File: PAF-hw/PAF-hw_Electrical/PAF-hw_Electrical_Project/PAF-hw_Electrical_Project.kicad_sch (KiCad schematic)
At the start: 0 parts

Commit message: Initial commit of schematic. Added ESP32 module. MicroUSB, and USB-C circuits to schematic.
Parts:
- added C1, C2: 10uF, CAPC2012X145N, symbol SamacSys_Parts:CL21A106KAYNNNE
- added D1, D5: 1N5819HWQ-7-F, SOD3716X145N, symbol SamacSys_Parts:1N5819HWQ-7-F
- added D2, D3, D4, D6, D7, D8: ESDLC5V0D3B-TP, SOD2512X115N, symbol SamacSys_Parts:ESDLC5V0D3B-TP
- added J1: USB_B_Micro, symbol Connector:USB_B_Micro
- added J2: USB_C_Receptacle_USB2.0_16P, symbol Connector:USB_C_Receptacle_USB2.0_16P
- added R1, R2: 5.1k, symbol Device:R
- added U1: ESP32-S3-WROOM-1, PCM_Espressif:ESP32-S3-WROOM-1, symbol PCM_Espressif:ESP32-S3-WROOM-1
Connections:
- new net: J2.B5 (CC2), R1.1
- new net: J2.A5 (CC1), R2.1
- new net +5V: C1.1, C2.1, D1.1 (K), D5.1 (K)
- new net D_N: D4.1 (K1), J1.2 (D-)
- new net D_P: D3.1 (K1), J1.3 (D+)
- new net EN: U1.3 (EN)
- new net ESP32_3V3: U1.2 (3V3)
- new net GND: C1.2, C2.2, D2.2 (K2), D3.2 (K2), D4.2 (K2), D6.2 (K2), D7.2 (K2), D8.2 (K2), J1.5 (GND), J1.6 (Shield), J2.A1 (GND), J2.A12 (GND), J2.B1 (GND), J2.B12 (GND), J2.S1 (SHIELD), R1.2, R2.2, U1.1 (GND), U1.40 (GND), U1.41 (GND)
- new net GPIO19/D_N: D8.1 (K1), J2.A7 (D-), J2.B7 (D-), U1.13 (GPIO19/U1RTS/ADC2_CH8/CLK_OUT2/USB_D-)
- new net GPIO20/D_P: D7.1 (K1), J2.A6 (D+), J2.B6 (D+), U1.14 (GPIO20/U1CTS/ADC2_CH9/CLK_OUT1/USB_D+)
- new net VBUS: D1.2 (A), D2.1 (K1), J1.1 (VBUS)
- new net VBUS_B: D5.2 (A), D6.1 (K1), J2.A4 (VBUS), J2.A9 (VBUS), J2.B4 (VBUS), J2.B9 (VBUS)
- no-connect marks 0 -> 3

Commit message: Added LDO and reset/boot swtiches to schematic.
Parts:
- added C3, C7: 10uF, CAPC2012X145N, symbol SamacSys_Parts:CL21A106KAYNNNE
- added C4, C5, C6, C8: 0.1uF, C0603, symbol SamacSys_Parts:C0603C104K5RACTU
- added IC1: NCP1117IST33T3G, SOT230P700X180-4N, symbol SamacSys_Parts:NCP1117IST33T3G
- added LED1: RED LED, SMLLX0805SRCTR, symbol SamacSys_Parts:SML-LX0805SRC-TR
- added R3: 5.1k, symbol Device:R
- added S1, S2: PTS647SK38SMTR2_LFS, PTS647SM38SMTR2LFS, symbol SamacSys_Parts:PTS647SK38SMTR2_LFS
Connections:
- net +5V: now also C3.1, C4.1, IC1.3 (INPUT_1)
- net EN: now also C6.2, S2.1 (NO_1), S2.2 (NO_2)
- net GND: now also R1.1, R2.1, C3.2, C4.2, C5.1, C6.1, C7.2, C8.2, IC1.1 (ADJUST/GROUND), LED1.2 (K), S1.3 (COM_1), S1.4 (COM_2), S2.3 (COM_1), S2.4 (COM_2); no longer R1.2, R2.2
- net at J2.B5 (CC2): now also R1.2; no longer R1.1
- net GPIO0/BOOT: now reaches U1.27 (GPIO0/BOOT)
- net GPIO0/BOOT: now also C5.2, S1.1 (NO_1), S1.2 (NO_2)
- net at J2.A5 (CC1): now also R2.2; no longer R2.1
- net ESP32_3V3 renamed +3.3V
- net +3.3V: now also C7.1, C8.1, IC1.2 (OUTPUT), IC1.4 (INPUT_2), R3.1
- new net: LED1.1 (A), R3.2
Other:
- moved on the sheet: C1, R1, R2, U1

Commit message: Added USB to UART and automatic boot logic to schematic.
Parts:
- added C10, C12: 10uF, CAPC2012X145N, symbol SamacSys_Parts:CL21A106KAYNNNE
- added C11: 0.1uF, C0603, symbol SamacSys_Parts:C0603C104K5RACTU
- added C13, C9: 1uF, CAPC1608X90N, symbol SamacSys_Parts:CL10B105KO8NNNC
- added IC2: CP2102N-A02-GQFN28R, QFN50P500X500X80-29N-D, symbol SamacSys_Parts:CP2102N-A02-GQFN28R
- added Q1, Q2: BC818-25, SOT95P230X110-3N, symbol SamacSys_Parts:BC818-25
- added R10, R12, R4, R8: 10k, symbol Device:R
- added R11, R13, R14, R15, R9: 0, symbol Device:R
- added R5: 22.1k, symbol Device:R
- added R6: 47.5k, symbol Device:R
- added R7: 1k, symbol Device:R
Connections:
- net +3.3V: now also C10.1, C11.1, C12.1, IC2.6 (VDD), IC2.7 (VREGIN), R15.1, R15.2, R4.1, R7.1
- net D_N: now also IC2.5 (D-)
- net D_P: now also IC2.4 (D+)
- net EN: now also C6.1, C9.1, R13.1, R4.2; no longer C6.2
- net GND: now also C6.2, C10.2, C11.2, C12.2, C13.2, C9.2, IC2.29 (GND_2), IC2.3 (GND_1), R6.2, R8.1; no longer C6.1
- net GPIO0/BOOT: now also R14.1
- net VBUS: now also R5.2
- net U0RXD: now reaches U1.36 (U0RXD/GPIO44/CLK_OUT2)
- net U0RXD: now also R9.1
- net U0TXD: now reaches U1.37 (U0TXD/GPIO43/CLK_OUT1)
- net U0TXD: now also R11.1
- new net: IC2.26 (TXD), R9.2
- new net: Q2.1 (B), R12.1
- new net: Q2.3 (C), R14.2
- new net: IC2.9 (RSTB), R7.2
- new net: IC2.11 (SUSPENDB), R8.2
- new net: IC2.25 (RXD), R11.2
- new net: C13.1, IC2.8 (VBUS), R5.1, R6.1
- new net: Q1.1 (B), R10.1
- new net: Q1.3 (C), R13.2
- new net DTR: IC2.28 (DTR), Q2.2 (E), R10.2
- new net RTS: IC2.24 (RTS), Q1.2 (E), R12.2
- no-connect marks 3 -> 18
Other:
- moved on the sheet: C5, C6, S1, S2, U1

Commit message: Added 12V input to the schematic, and simulated soft start circuit.
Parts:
- added C14: 10uF, CAPC2012X145N, symbol SamacSys_Parts:CL21A106KAYNNNE
- added D9: ESD12VD3B-TP, SOD2512X115N, symbol SamacSys_Parts:ESD12VD3B-TP
- added J3: Barrel_Jack_Switch, symbol Connector:Barrel_Jack_Switch
- added LED2: GREEN LED, LEDC2012X120N, symbol SamacSys_Parts:LTST-C170GKT
- added R16: 300, symbol Device:R
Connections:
- net GND: now also C14.2, D9.2, J3.2, J3.3, LED2.1 (K)
- net GPIO21: now reaches U1.23 (GPIO21)
- net GPIO21: now also R16.2
- new net: LED2.2 (A), R16.1
- new net +12V: C14.1, D9.1, J3.1
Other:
- moved on the sheet: C1, C10, C11, C12, C13, C2, C3, C4, C5, C6, C7, C8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

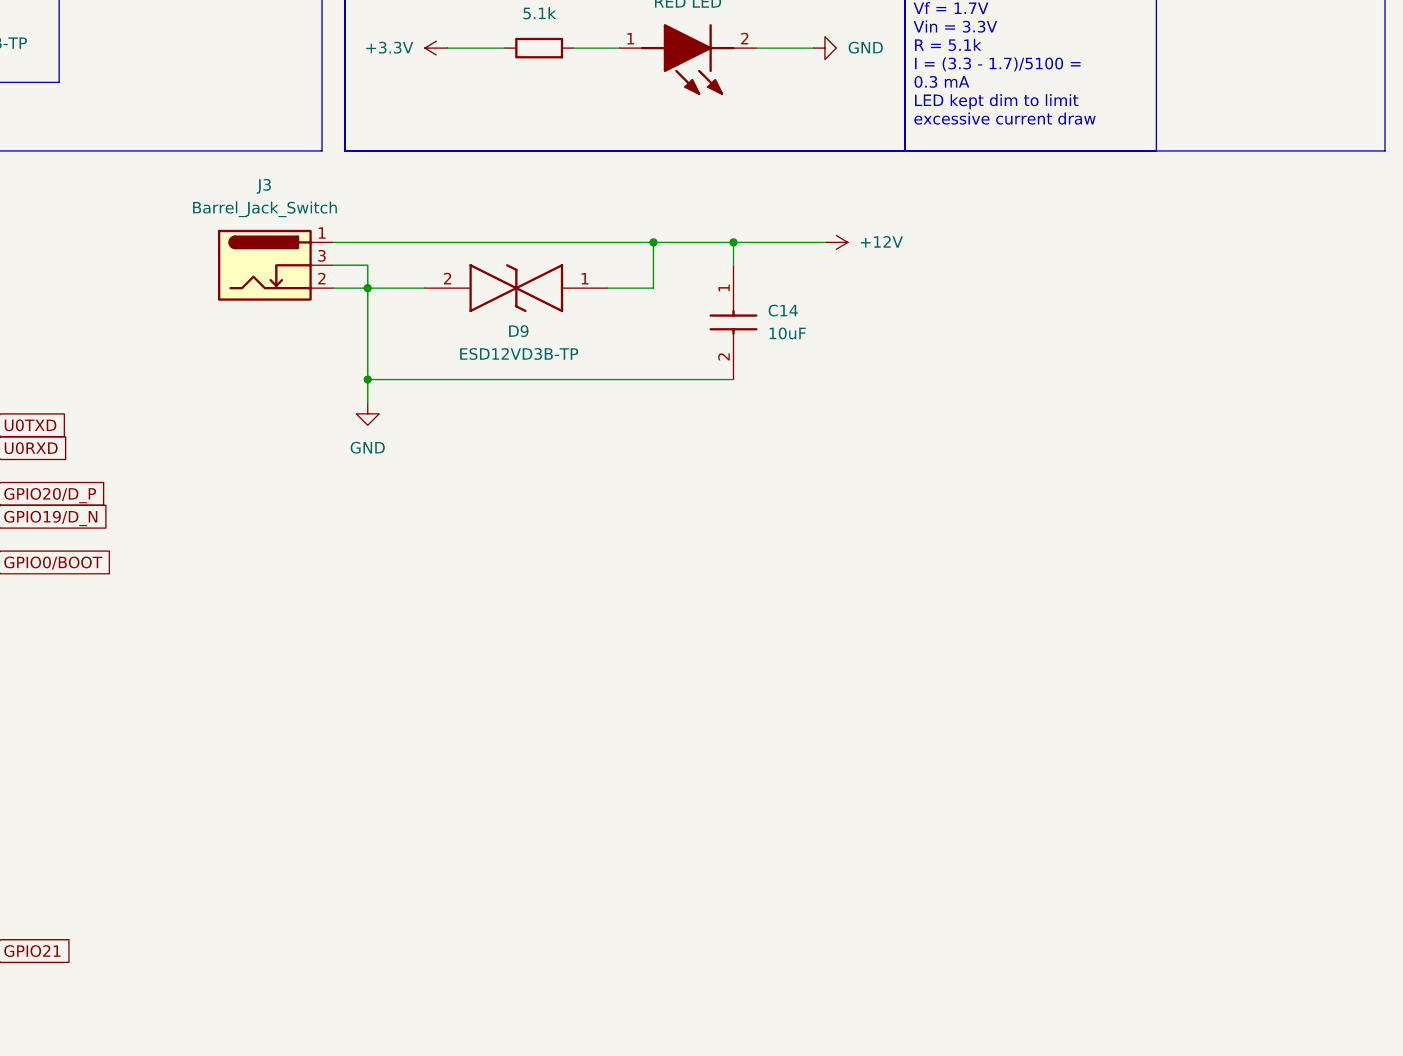
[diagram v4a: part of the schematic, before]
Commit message: Added soft start on 12V rail to schematic.
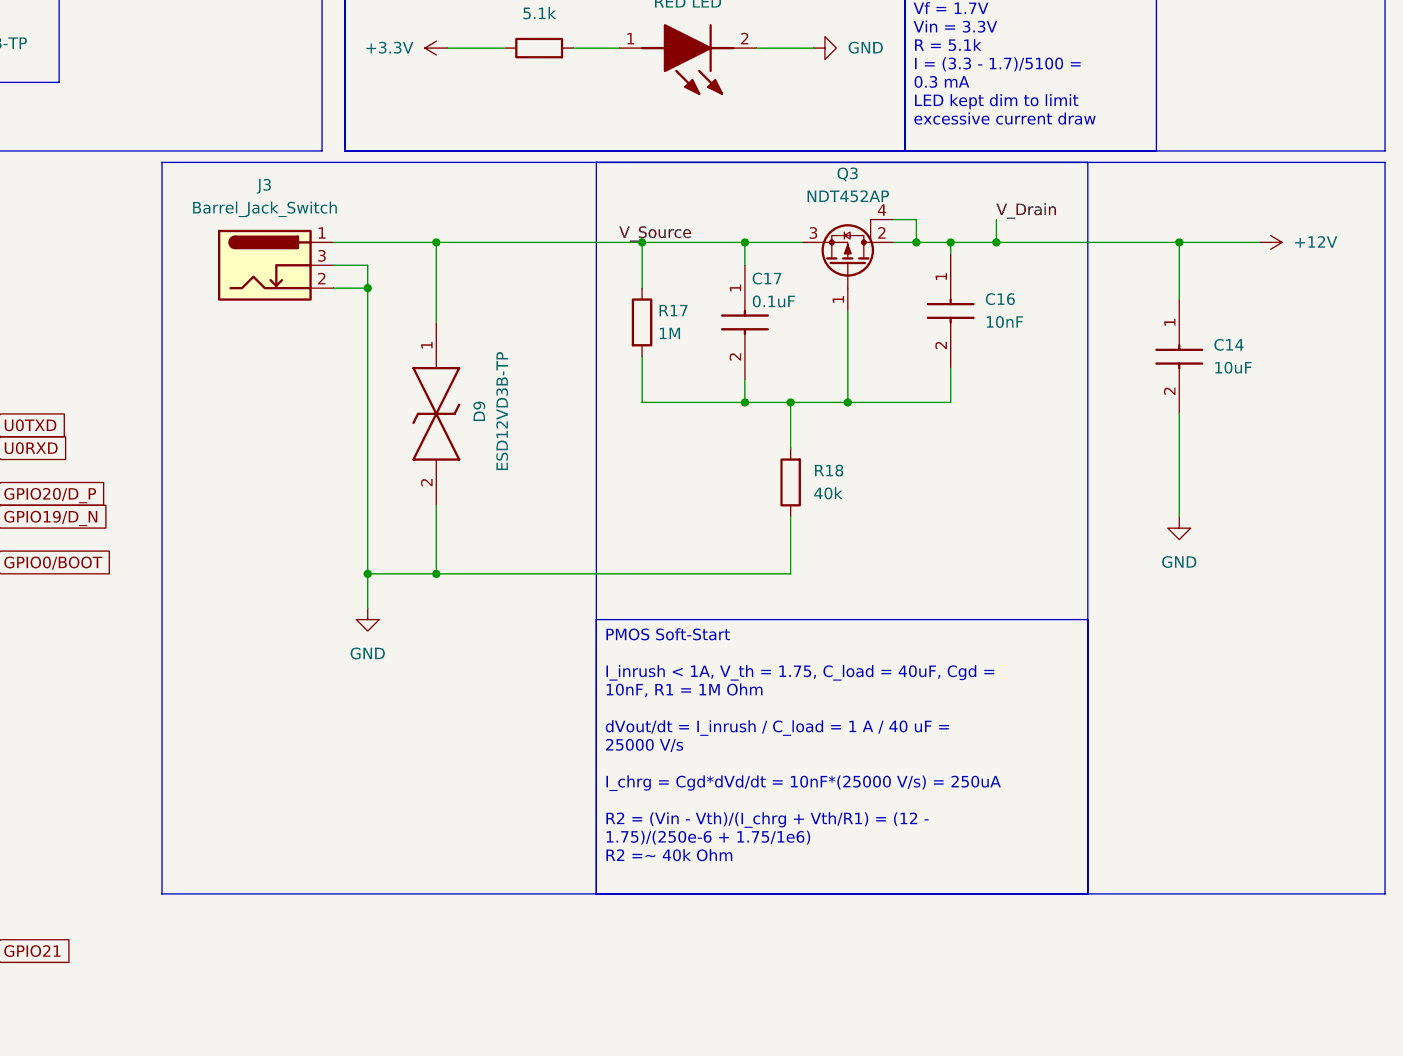
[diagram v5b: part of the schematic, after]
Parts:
- added C16: 10nF, CAPC1005X70N, symbol SamacSys_Parts:GRM155R71E103KA01D
- added C17: 0.1uF, C0603, symbol SamacSys_Parts:C0603C104K5RACTU
- added Q3: NDT452AP, SamacSys_Parts:SOT230P700X180-4N, symbol Transistor_FET:Q_PMOS_GDSD
- added R17: 1M, symbol Device:R
- added R18: 40k, symbol Device:R
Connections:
- net +12V: now also C16.1, Q3.2 (D), Q3.4 (D); no longer D9.1, J3.1
- net GND: now also R18.1
- new net: C16.2, C17.2, Q3.1 (G), R17.2, R18.2
- new net V_Source: C17.1, D9.1, J3.1, Q3.3 (S), R17.1
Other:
- moved on the sheet: D9

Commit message: Added 12V to 5V switching regulator to schematic and converted all modules to hiearchal schematics.
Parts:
- removed C1, C12, C14, C2, C3, C7: 10uF, CAPC2012X145N, symbol SamacSys_Parts:CL21A106KAYNNNE
- removed C13, C9: 1uF, CAPC1608X90N, symbol SamacSys_Parts:CL10B105KO8NNNC
- removed C16: 10nF, CAPC1005X70N, symbol SamacSys_Parts:GRM155R71E103KA01D
- removed C17, C4, C5, C6, C8: 0.1uF, C0603, symbol SamacSys_Parts:C0603C104K5RACTU
- removed D1, D5: 1N5819HWQ-7-F, SOD3716X145N, symbol SamacSys_Parts:1N5819HWQ-7-F
- removed D2, D3, D4, D6, D7, D8: ESDLC5V0D3B-TP, SOD2512X115N, symbol SamacSys_Parts:ESDLC5V0D3B-TP
- removed D9: ESD12VD3B-TP, SOD2512X115N, symbol SamacSys_Parts:ESD12VD3B-TP
- removed IC1: NCP1117IST33T3G, SOT230P700X180-4N, symbol SamacSys_Parts:NCP1117IST33T3G
- removed IC2: CP2102N-A02-GQFN28R, QFN50P500X500X80-29N-D, symbol SamacSys_Parts:CP2102N-A02-GQFN28R
- removed J1: USB_B_Micro, symbol Connector:USB_B_Micro
- removed J2: USB_C_Receptacle_USB2.0_16P, symbol Connector:USB_C_Receptacle_USB2.0_16P
- removed J3: Barrel_Jack_Switch, symbol Connector:Barrel_Jack_Switch
- removed LED1: RED LED, SMLLX0805SRCTR, symbol SamacSys_Parts:SML-LX0805SRC-TR
- removed Q1, Q2: BC818-25, SOT95P230X110-3N, symbol SamacSys_Parts:BC818-25
- removed Q3: NDT452AP, SamacSys_Parts:SOT230P700X180-4N, symbol Transistor_FET:Q_PMOS_GDSD
- removed R1, R2, R3: 5.1k, symbol Device:R
- removed R10, R12, R4, R8: 10k, symbol Device:R
- removed R11, R13, R14, R9: 0, symbol Device:R
- removed R17: 1M, symbol Device:R
- removed R18: 40k, symbol Device:R
- removed R5: 22.1k, symbol Device:R
- removed R6: 47.5k, symbol Device:R
- removed R7: 1k, symbol Device:R
- removed S1, S2: PTS647SK38SMTR2_LFS, PTS647SM38SMTR2LFS, symbol SamacSys_Parts:PTS647SK38SMTR2_LFS
- added J5: Barrel_Jack_Switch, symbol Connector:Barrel_Jack_Switch
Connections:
- net GND: now also J5.2, J5.3
- new net BARREL_12V: J5.1
- no-connect marks 18 -> 0
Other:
- added sheet 12V-5V SW REG (12V-5V_SW_REG.kicad_sch)
- added sheet 5V-3.3V LDO (5V-3.3V_LDO.kicad_sch)
- added sheet Auto_Reset (Auto_Reset.kicad_sch)
- added sheet MicroUSB (MicroUSB.kicad_sch)
- added sheet Reset and Boot Switches (Reset_Boot_Switches.kicad_sch)
- added sheet Soft_Start (Soft_Start.kicad_sch)
- added sheet USB-C (USB-C.kicad_sch)
- added sheet USB-UART (USB-UART.kicad_sch)
- moved on the sheet: C10, C11, R15, U1
